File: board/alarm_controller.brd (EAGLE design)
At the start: 90 x 65 mm, 138 parts, among them IC3 AT24C, X1 RJ45-8L21-S, X2 RJ45-8L21-S

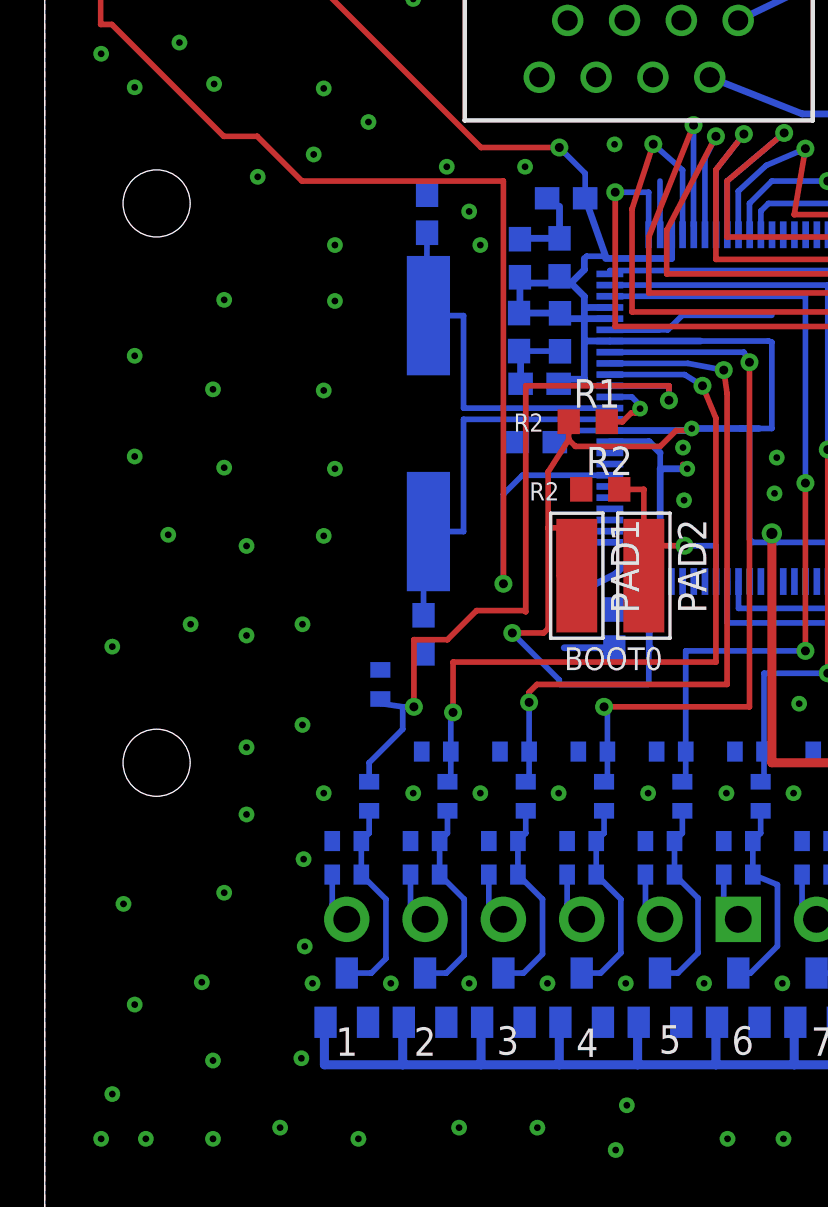
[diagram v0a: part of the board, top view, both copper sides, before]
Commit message: add reset button
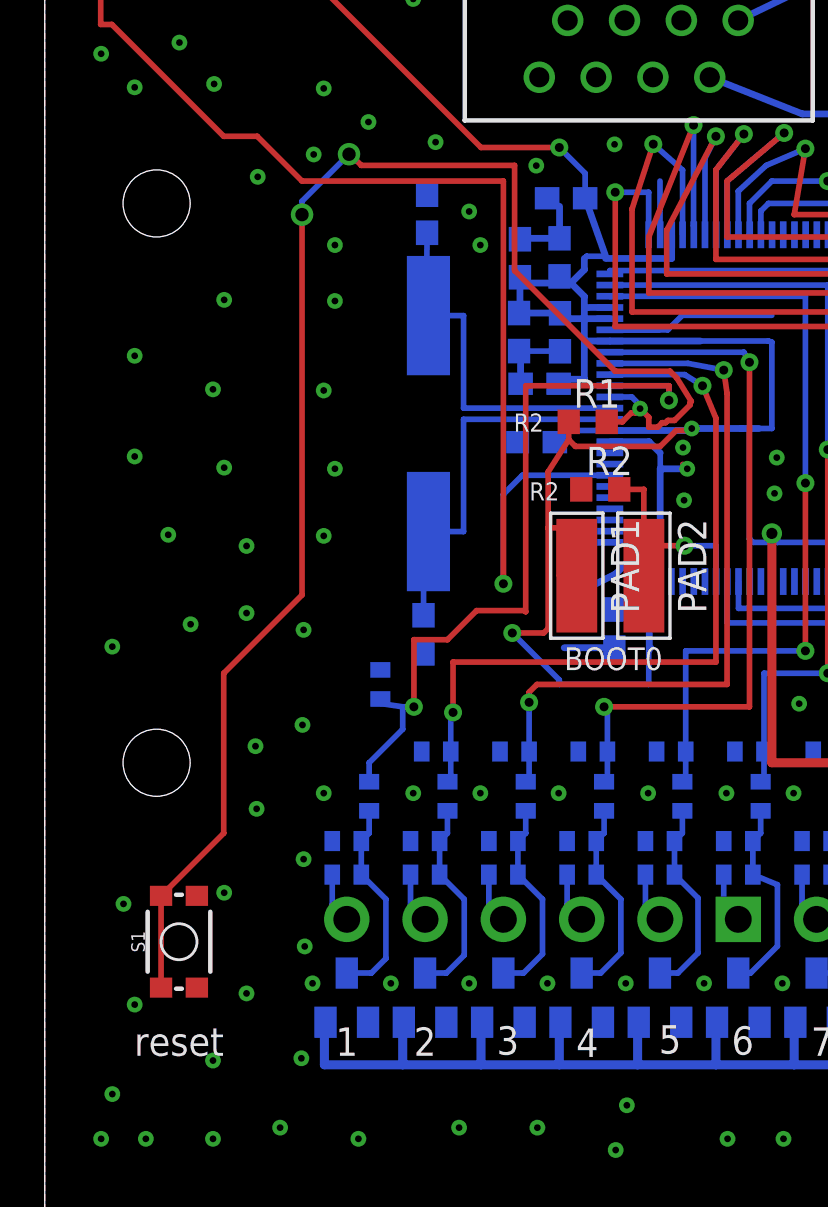
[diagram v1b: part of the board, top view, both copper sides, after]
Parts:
- added S1: (no value), SparkFun-Switches:TACTILE_SWITCH_SMD_4.6X2.8MM
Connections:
- removed net N$5: R1.2, U$1.NRST
- new net N$7: R1.2, S1.3, S1.4, U$1.NRST
- net GND: now also S1.1, S1.2
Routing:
- net N$7: track 0.00 -> 70.3 mm, vias 0 -> 3
- net N$5: track 3.39 -> 0.00 mm, vias 1 -> 0
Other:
- board text added: "reset"
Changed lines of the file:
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@@
 <wire x1="82.65" y1="27.35" x2="62.4" y2="27.35" width="0.4064" layer="121"/>
 <wire x1="62.4" y1="27.35" x2="62.4" y2="37.5" width="0.4064" layer="121"/>
+<text x="4" y="6.9" size="1.27" layer="121">reset</text>
 </plain>
 <attributes>
@@
 <element name="U$2" library="mounting" package="DIN-MOUNT-2-HOLE" value="" x="5" y="32.5"/>
 <element name="U$3" library="mounting" package="DIN-MOUNT-2-HOLE" value="" x="85" y="32.5"/>
+<element name="S1" library="SparkFun-Switches" package="TACTILE_SWITCH_SMD_4.6X2.8MM" value="" x="6" y="12" rot="R90">
+<attribute name="PROD_ID" value="SWCH-13065" x="6" y="12" size="1.778" layer="27" rot="R90" display="off"/>
+</element>
 </elements>
 <signals>
@@
 <via x="12.97" y="33.14" extent="1-16" drill="0.3" diameter="0.3048"/>
 <via x="12.47" y="30.14" extent="1-16" drill="0.3" diameter="0.3048"/>
-<via x="17.97" y="46.64" extent="1-16" drill="0.3" diameter="0.3048"/>
+<via x="17.47" y="47.74" extent="1-16" drill="0.3" diameter="0.3048"/>
 <via x="12.47" y="50.14" extent="1-16" drill="0.3" diameter="0.3048"/>
 <via x="16.47" y="54.14" extent="1-16" drill="0.3" diameter="0.3048"/>
@@
 <wire x1="49.04" y1="44.96" x2="48.5" y2="45.5" width="0.254" layer="1"/>
 <via x="18.97" y="44.64" extent="1-16" drill="0.3" diameter="0.3048"/>
-<via x="21.47" y="46.64" extent="1-16" drill="0.3" diameter="0.3048"/>
+<via x="21.97" y="46.69" extent="1-16" drill="0.3" diameter="0.3048"/>
 <wire x1="25.26" y1="39.35" x2="27.85" y2="39.35" width="0.254" layer="16"/>
 <wire x1="27.85" y1="39.35" x2="28.5" y2="40" width="0.254" layer="16"/>
@@
 <via x="3.02" y="5.19" extent="1-16" drill="0.3" diameter="0.3048"/>
 <via x="7.52" y="6.69" extent="1-16" drill="0.3" diameter="0.3048"/>
-<via x="7.02" y="10.19" extent="1-16" drill="0.3" diameter="0.3048"/>
+<via x="9.02" y="9.69" extent="1-16" drill="0.3" diameter="0.3048"/>
 <via x="4.02" y="9.19" extent="1-16" drill="0.3" diameter="0.3048"/>
 <via x="3.52" y="13.69" extent="1-16" drill="0.3" diameter="0.3048"/>
 <via x="8.02" y="14.19" extent="1-16" drill="0.3" diameter="0.3048"/>
-<via x="9.02" y="17.69" extent="1-16" drill="0.3" diameter="0.3048"/>
-<via x="9.02" y="20.69" extent="1-16" drill="0.3" diameter="0.3048"/>
+<via x="9.47" y="17.94" extent="1-16" drill="0.3" diameter="0.3048"/>
+<via x="9.42" y="20.74" extent="1-16" drill="0.3" diameter="0.3048"/>
 <via x="11.52" y="21.69" extent="1-16" drill="0.3" diameter="0.3048"/>
-<via x="11.52" y="26.19" extent="1-16" drill="0.3" diameter="0.3048"/>
-<via x="9.02" y="25.69" extent="1-16" drill="0.3" diameter="0.3048"/>
+<via x="11.57" y="25.94" extent="1-16" drill="0.3" diameter="0.3048"/>
+<via x="9.02" y="26.69" extent="1-16" drill="0.3" diameter="0.3048"/>
 <via x="6.52" y="26.19" extent="1-16" drill="0.3" diameter="0.3048"/>
 <via x="9.02" y="29.69" extent="1-16" drill="0.3" diameter="0.3048"/>
@@
 <contactref element="U$4" pad="GND"/>
 <via x="14.47" y="48.64" extent="1-16" drill="0.3" diameter="0.3048"/>
+<contactref element="S1" pad="1"/>
+<contactref element="S1" pad="2"/>
 </signal>
 <signal name="+3V3">
@@
 <wire x1="26.78" y1="32.22" x2="26.78" y2="29.7" width="0.254" layer="1"/>
 </signal>
-<signal name="N$5">
-<contactref element="U$1" pad="NRST"/>
-<contactref element="R1" pad="2"/>
-<wire x1="25.26" y1="36.35" x2="26.24" y2="36.35" width="0.254" layer="16"/>
-<wire x1="26.24" y1="36.35" x2="26.55" y2="36.04" width="0.254" layer="16"/>
-<wire x1="26.55" y1="36.04" x2="26.55" y2="35.89" width="0.254" layer="16"/>
-<wire x1="26.55" y1="35.89" x2="26.61" y2="35.83" width="0.254" layer="16"/>
-<via x="26.61" y="35.83" extent="1-16" drill="0.3"/>
-<wire x1="26.61" y1="35.83" x2="26.42" y2="35.64" width="0.254" layer="1"/>
-<wire x1="26.42" y1="35.64" x2="26.22" y2="35.64" width="0.254" layer="1"/>
-<wire x1="26.22" y1="35.64" x2="25.82" y2="35.24" width="0.254" layer="1"/>
-<wire x1="25.82" y1="35.24" x2="25.12" y2="35.24" width="0.254" layer="1"/>
-</signal>
 <signal name="A23">
 <contactref element="R6" pad="2"/>
@@
 <wire x1="63.61" y1="28.5" x2="63.61" y2="28.69" width="1.27" layer="1"/>
 </signal>
+<signal name="N$7">
+<contactref element="S1" pad="3"/>
+<contactref element="S1" pad="4"/>
+<contactref element="U$1" pad="NRST"/>
+<contactref element="R1" pad="2"/>
+<wire x1="25.26" y1="36.35" x2="26.24" y2="36.35" width="0.254" layer="16"/>
+<wire x1="26.24" y1="36.35" x2="26.55" y2="36.04" width="0.254" layer="16"/>
+<wire x1="26.55" y1="36.04" x2="26.55" y2="35.89" width="0.254" layer="16"/>
+<wire x1="26.55" y1="35.89" x2="26.61" y2="35.83" width="0.254" layer="16"/>
+<via x="26.61" y="35.83" extent="1-16" drill="0.3"/>
+<wire x1="26.61" y1="35.83" x2="26.42" y2="35.64" width="0.254" layer="1"/>
+<wire x1="26.42" y1="35.64" x2="26.22" y2="35.64" width="0.254" layer="1"/>
+<wire x1="26.22" y1="35.64" x2="25.82" y2="35.24" width="0.254" layer="1"/>
+<wire x1="25.82" y1="35.24" x2="25.12" y2="35.24" width="0.254" layer="1"/>
+<wire x1="26.61" y1="35.83" x2="27" y2="35.44" width="0.254" layer="1"/>
+<wire x1="27" y1="35.44" x2="27" y2="35" width="0.254" layer="1"/>
+<wire x1="27" y1="35" x2="27.4" y2="35" width="0.254" layer="1"/>
+<wire x1="27.4" y1="35" x2="27.6" y2="35.2" width="0.254" layer="1"/>
+<wire x1="27.6" y1="35.2" x2="27.75" y2="35.2" width="0.254" layer="1"/>
+<wire x1="27.75" y1="35.2" x2="27.85" y2="35.3" width="0.254" layer="1"/>
+<wire x1="27.85" y1="35.3" x2="28.15" y2="35.3" width="0.254" layer="1"/>
+<wire x1="28.15" y1="35.3" x2="28.85" y2="36" width="0.254" layer="1"/>
+<wire x1="28.85" y1="36" x2="28.85" y2="36.1" width="0.254" layer="1"/>
+<wire x1="28.85" y1="36.1" x2="28.9" y2="36.15" width="0.254" layer="1"/>
+<wire x1="28.9" y1="36.15" x2="28.25" y2="37.2" width="0.254" layer="1"/>
+<wire x1="28.25" y1="37.2" x2="27.95" y2="37.5" width="0.254" layer="1"/>
+<wire x1="27.95" y1="37.5" x2="25.5" y2="37.5" width="0.254" layer="1"/>
+<wire x1="25.5" y1="37.5" x2="21" y2="42" width="0.254" layer="1"/>
+<wire x1="21" y1="42" x2="21" y2="46.7" width="0.254" layer="1"/>
+<wire x1="21" y1="46.7" x2="14.15" y2="46.7" width="0.254" layer="1"/>
+<wire x1="14.15" y1="46.7" x2="13.65" y2="47.2" width="0.254" layer="1"/>
+<wire x1="13.65" y1="47.2" x2="13.6" y2="47.2" width="0.254" layer="1"/>
+<via x="13.6" y="47.2" extent="1-16" drill="0.6"/>
+<wire x1="13.6" y1="47.2" x2="11.5" y2="45.1" width="0.254" layer="16"/>
+<wire x1="11.5" y1="45.1" x2="11.5" y2="44.5" width="0.254" layer="16"/>
+<via x="11.5" y="44.5" extent="1-16" drill="0.6"/>
+<wire x1="5.2" y1="9.95" x2="5.2" y2="14.05" width="0.254" layer="1"/>
+<wire x1="5.2" y1="14.05" x2="8" y2="16.85" width="0.254" layer="1"/>
+<wire x1="11.5" y1="27.5" x2="11.5" y2="44.5" width="0.254" layer="1"/>
+<wire x1="8" y1="16.85" x2="8" y2="24" width="0.254" layer="1"/>
+<wire x1="8" y1="24" x2="11.5" y2="27.5" width="0.254" layer="1"/>
+</signal>
 </signals>
+<errors>
+</errors>
 </board>
 </drawing>

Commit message: fix tamper
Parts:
- added J1: (no value), SparkFun-Connectors:1X02
- added R35: 10k, rcl:R0603
- added S2: (no value), SparkFun-Switches:TACTILE_SWITCH_SMD_4.6X2.8MM
- moved R61 1.12 mm to (58.5, 53.5), turned to 270 degrees
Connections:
- new net HARDWARE_RESET: R35.2, S2.3, S2.4, U$1.PE0
- new net UART_RX: J1.1, U$1.PA10
- new net UART_TX: J1.2, U$1.PA9
- net +3V3: now also R35.1
- net ASDASD: no longer U$1.PB12
- net GND: now also S2.1, S2.2
- net TAMPER: now also U$1.PB12
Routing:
- net HARDWARE_RESET: track 0.00 -> 31.5 mm, vias 0 -> 1
- net UART_TX: track 0.00 -> 28.7 mm
- net UART_RX: track 0.00 -> 26.1 mm
- net ASDASD: track 32.9 -> 6.84 mm, vias 2 -> 0
- net +3V3: track 420.3 -> 446.2 mm
- net TAMPER: track 0.00 -> 24.8 mm, vias 0 -> 2
- net GND: track 62.0 -> 66.0 mm, vias 182 -> 185
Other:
- board text added: "RX"
- board text added: "TX"
- board text added: "UART"
- board text added: "factory reset"
- board text removed: "IN"
- board text removed: "OUT"

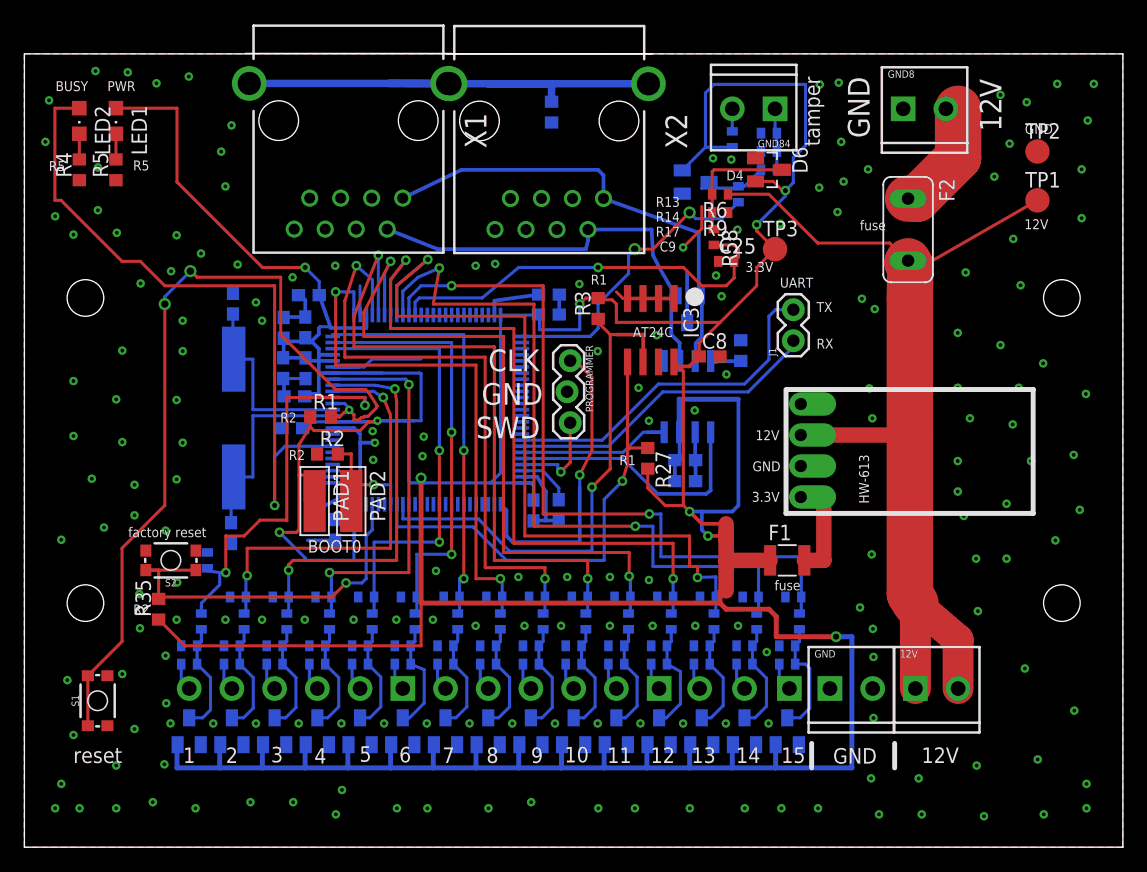
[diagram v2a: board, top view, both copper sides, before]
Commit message: power over can
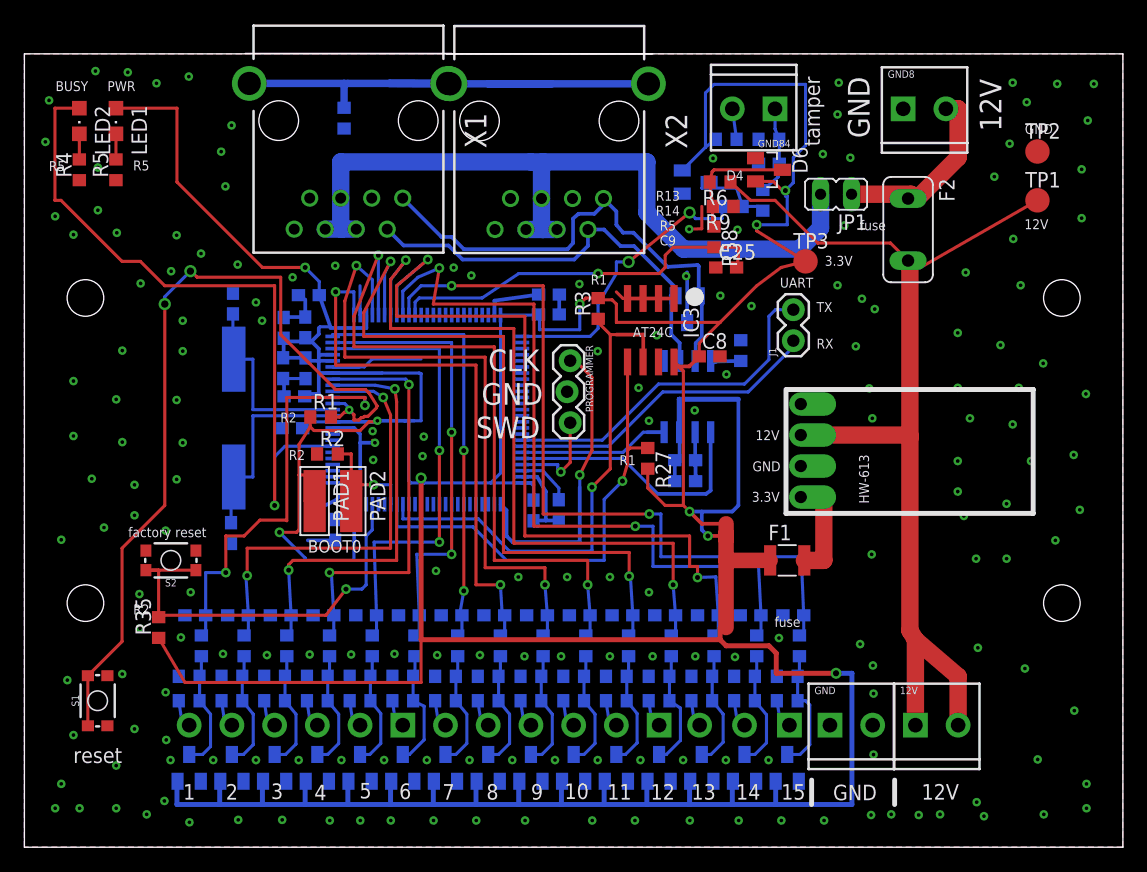
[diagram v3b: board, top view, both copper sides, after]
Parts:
- added JP1: (no value), jumper:JP1
- C11, C2, C24, C25, C27, C28, C29, C30, C31, C32, C33, C34, C35, C36, C37, C38, C39: device eagle-ltspice:C0402 -> eagle-ltspice:C0603
- R10, R11, R12, R13, R14, R15, R16, R17, R18, R19, R20, R21, R22, R23, R26, R28, R29, R30, R31, R32, R33, R34, R37, R38, R39, R40, R41, R42, R43, R44, R45, R46, R47, R48, R49, R50, R51, R52, R53, R54, R55, R56, R57, R58, R59, R6, R60, R61, R62, R7, R8, R9: device rcl:R0402 -> rcl:R0603
- moved R25 17.0 mm to (26.2, 59.7)
- moved C11 4.61 mm to (14.0, 19.0), turned to 180 degrees
- moved 12V 3.00 mm to (73.0, 10.0)
- moved ALARMS 3.00 mm to (52.0, 10.0)
- moved ALARMS1 3.00 mm to (31.0, 10.0)
- moved ALARMS2 3.00 mm to (62.5, 10.0)
- moved D1 3.00 mm to (13.5, 6.50)
- moved D10 3.00 mm to (38.0, 6.50)
- moved D11 3.00 mm to (41.5, 6.50)
- moved D12 3.00 mm to (45.0, 6.50)
- moved D13 3.00 mm to (48.5, 6.50)
- moved D14 3.00 mm to (52.0, 6.50)
- moved D15 3.00 mm to (55.5, 6.50)
- moved D16 3.00 mm to (59.0, 6.50)
- moved D17 3.00 mm to (62.5, 6.50)
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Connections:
- removed net N$14: F2.1, GND8.2
- new net PRE_FUSE_12V: F2.1, GND8.2, JP1.1
- new net RJ45_12V: JP1.2, X1.4, X1.5, X1.6, X2.4, X2.5, X2.6
- net GND: now also X1.8, X2.8
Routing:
- net RJ45_12V: track 0.00 -> 64.4 mm
- net PRE_FUSE_12V: track 0.00 -> 15.9 mm
- net +3V3: track 446.2 -> 457.5 mm
- net N$14: track 10.5 -> 0.00 mm
- net +12V: track 92.9 -> 85.2 mm
- net HARDWARE_RESET: track 31.5 -> 34.7 mm
- net N$11: track 5.03 -> 7.40 mm
- net ALARM_REFERENCE: track 33.8 -> 31.4 mm
- net ALARM_8: track 43.5 -> 45.6 mm
- net CAN_H: track 38.2 -> 40.3 mm
- net ALARM_9: track 49.8 -> 51.8 mm
- net ALARM_12: track 57.5 -> 59.6 mm
- net ALARM_10: track 53.9 -> 55.9 mm
- net ALARM_13: track 62.2 -> 64.3 mm
- net ALARM_11: track 55.8 -> 57.9 mm
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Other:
- board text added: "C9 R5 R14 R13 D4"
- board text added: "R13 R14 R5 C9"
- board text added: "alarm controller 2020.06.11 v1.3"
- board text removed: "2020.05.08 v1.2"
- board text removed: "C9 R17 R14 R13 D4"
- board text removed: "R13 R14 R17 C9"
